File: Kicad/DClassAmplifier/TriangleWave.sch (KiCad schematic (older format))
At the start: 7 parts, among them U2 MAX4016ESA+

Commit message: Combined Board
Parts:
- C13: renamed from CF2; footprint Capacitor_SMD:C_0805_2012Metric_Pad1.18x1.45mm_HandSolder -> Capacitor_SMD:C_0603_1608Metric_Pad1.08x0.95mm_HandSolder
- C14: renamed from C5; footprint Capacitor_SMD:C_0201_0603Metric_Pad0.64x0.40mm_HandSolder -> Capacitor_SMD:C_0603_1608Metric_Pad1.08x0.95mm_HandSolder
- renumbered R4 to R22, R3 to R23, R5 to R24, R6 to R25, U2 to U4
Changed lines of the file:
@@
 $EndDescr
 $Comp
-L power:VCC #PWR015
+L power:VCC #PWR039
 U 1 1 610A2484
 P 6500 3450
-F 0 "#PWR015" H 6500 3300 50  0001 C CNN
+F 0 "#PWR039" H 6500 3300 50  0001 C CNN
 F 1 "VCC" H 6515 3623 50  0000 C CNN
 F 2 "" H 6500 3450 50  0001 C CNN
@@
 $EndComp
 $Comp
-L power:GND #PWR014
+L power:GND #PWR041
 U 1 1 610A5C03
 P 4100 4100
-F 0 "#PWR014" H 4100 3850 50  0001 C CNN
+F 0 "#PWR041" H 4100 3850 50  0001 C CNN
 F 1 "GND" H 4105 3927 50  0000 C CNN
 F 2 "" H 4100 4100 50  0001 C CNN
@@
 TRIANGLE_OUT
 $Comp
-L Device:R_Small R4
+L Device:R_Small R22
 U 1 1 610ABFC7
 P 5300 2850
-F 0 "R4" V 5104 2850 50  0000 C CNN
+F 0 "R22" V 5104 2850 50  0000 C CNN
 F 1 "2.2k" V 5195 2850 50  0000 C CNN
 F 2 "Resistor_SMD:R_0603_1608Metric_Pad0.98x0.95mm_HandSolder" H 5300 2850 50  0001 C CNN
@@
 	4100 4100 4100 3750
 $Comp
-L Device:C_Small C5
+L Device:C_Small C14
 U 1 1 610B0597
 P 6850 3650
-F 0 "C5" V 6950 3575 50  0000 L CNN
+F 0 "C14" V 6950 3575 50  0000 L CNN
 F 1 "10n" V 7025 3575 50  0000 L CNN
-F 2 "Capacitor_SMD:C_0201_0603Metric_Pad0.64x0.40mm_HandSolder" H 6850 3650 50  0001 C CNN
+F 2 "Capacitor_SMD:C_0603_1608Metric_Pad1.08x0.95mm_HandSolder" H 6850 3650 50  0001 C CNN
 F 3 "~" H 6850 3650 50  0001 C CNN
 	1    6850 3650
@@
 	7000 3550 7100 3550
 $Comp
-L Device:R_Small R5
+L Device:R_Small R24
 U 1 1 610B770E
 P 5300 4600
-F 0 "R5" V 5104 4600 50  0000 C CNN
+F 0 "R24" V 5104 4600 50  0000 C CNN
 F 1 "12k" V 5195 4600 50  0000 C CNN
 F 2 "Resistor_SMD:R_0603_1608Metric_Pad0.98x0.95mm_HandSolder" H 5300 4600 50  0001 C CNN
@@
 	3900 3450 3500 3450
 $Comp
-L Device:R_Small R3
+L Device:R_Small R23
 U 1 1 610B9D20
 P 3500 3550
-F 0 "R3" H 3559 3596 50  0000 L CNN
+F 0 "R23" H 3559 3596 50  0000 L CNN
 F 1 "27k" H 3559 3505 50  0000 L CNN
 F 2 "Resistor_SMD:R_0603_1608Metric_Pad0.98x0.95mm_HandSolder" H 3500 3550 50  0001 C CNN
@@
 	6600 3650 6750 3650
 $Comp
-L Device:R_Small R6
+L Device:R_Small R25
 U 1 1 6110AB92
 P 5300 4950
-F 0 "R6" V 5104 4950 50  0000 C CNN
+F 0 "R25" V 5104 4950 50  0000 C CNN
 F 1 "12k" V 5195 4950 50  0000 C CNN
 F 2 "Resistor_SMD:R_0603_1608Metric_Pad0.98x0.95mm_HandSolder" H 5300 4950 50  0001 C CNN
@@
 	5050 4750 5050 4950
 $Comp
-L DClassAmplifier-rescue:MAX4016ESA+-MAX4016ESA U2
+L DClassAmplifier-rescue:MAX4016ESA+-MAX4016ESA U4
 U 1 1 610FB9E0
 P 4100 3450
-F 0 "U2" H 5300 3837 60  0000 C CNN
+F 0 "U4" H 5300 3837 60  0000 C CNN
 F 1 "MAX4016ESA+" H 5300 3731 60  0000 C CNN
 F 2 "MAX4016ESA:MAX4016ESA&plus_" H 5300 3690 60  0001 C CNN
@@
 $EndComp
 $Comp
-L Device:C_Small CF?
+L Device:C_Small C?
 U 1 1 611DAEFE
 P 6600 3450
-AR Path="/610C616D/611DAEFE" Ref="CF?"  Part="1"
-AR Path="/611D4178/611DAEFE" Ref="CF?"  Part="1"
-AR Path="/6109BB03/611DAEFE" Ref="CF2"  Part="1"
-F 0 "CF2" V 6371 3450 50  0000 C CNN
+AR Path="/610C616D/611DAEFE" Ref="C?"  Part="1"
+AR Path="/611D4178/611DAEFE" Ref="C?"  Part="1"
+AR Path="/6109BB03/611DAEFE" Ref="C13"  Part="1"
+F 0 "C13" V 6371 3450 50  0000 C CNN
 F 1 "100n" V 6462 3450 50  0000 C CNN
-F 2 "Capacitor_SMD:C_0805_2012Metric_Pad1.18x1.45mm_HandSolder" H 6600 3450 50  0001 C CNN
+F 2 "Capacitor_SMD:C_0603_1608Metric_Pad1.08x0.95mm_HandSolder" H 6600 3450 50  0001 C CNN
 F 3 "~" H 6600 3450 50  0001 C CNN
 	1    6600 3450
@@
 $EndComp
 $Comp
-L power:GND #PWR?
+L power:GND #PWR040
 U 1 1 611DAF04
 P 6700 3450
-F 0 "#PWR?" H 6700 3200 50  0001 C CNN
+F 0 "#PWR040" H 6700 3200 50  0001 C CNN
 F 1 "GND" H 6705 3277 50  0000 C CNN
 F 2 "" H 6700 3450 50  0001 C CNN

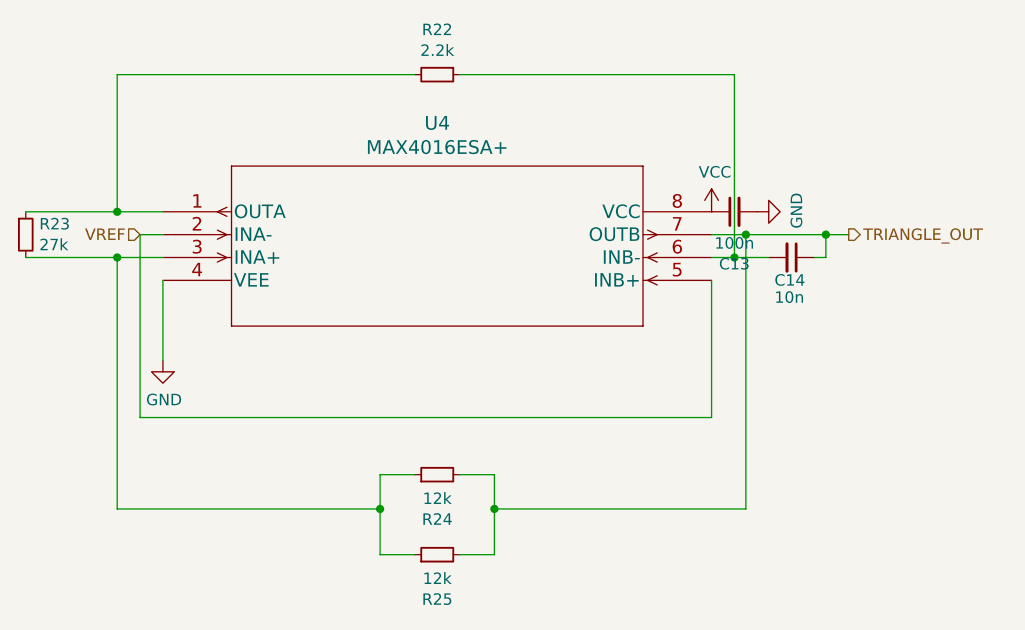
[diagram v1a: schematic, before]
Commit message: Add 10V Reg and Reroute
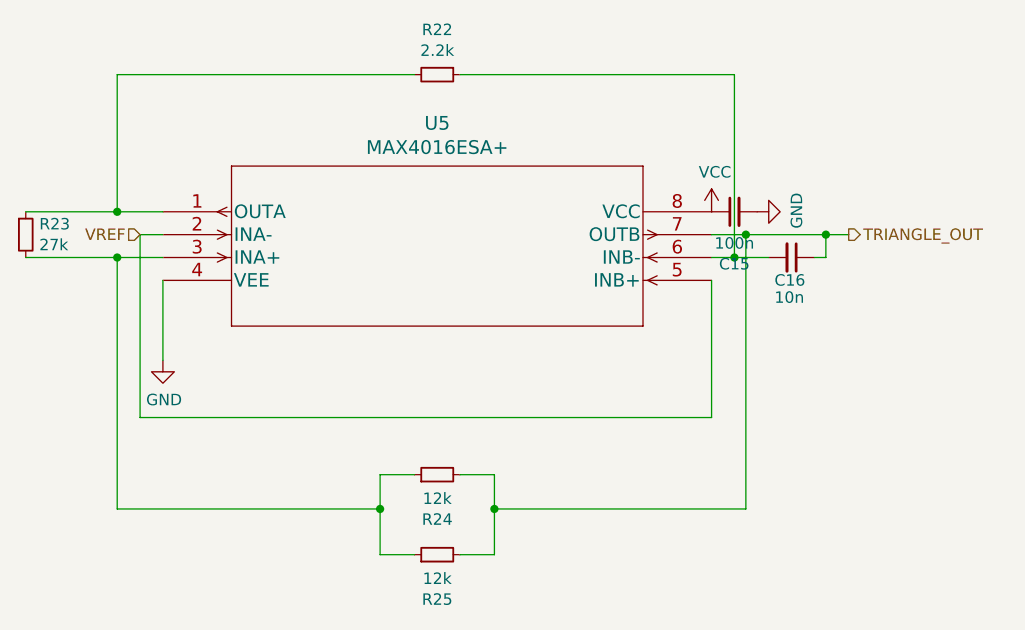
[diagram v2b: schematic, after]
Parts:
- renumbered C13 to C15, C14 to C16, U4 to U5
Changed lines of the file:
@@
 $EndDescr
 $Comp
-L power:VCC #PWR039
+L power:VCC #PWR042
 U 1 1 610A2484
 P 6500 3450
-F 0 "#PWR039" H 6500 3300 50  0001 C CNN
+F 0 "#PWR042" H 6500 3300 50  0001 C CNN
 F 1 "VCC" H 6515 3623 50  0000 C CNN
 F 2 "" H 6500 3450 50  0001 C CNN
@@
 $EndComp
 $Comp
-L power:GND #PWR041
+L power:GND #PWR044
 U 1 1 610A5C03
 P 4100 4100
-F 0 "#PWR041" H 4100 3850 50  0001 C CNN
+F 0 "#PWR044" H 4100 3850 50  0001 C CNN
 F 1 "GND" H 4105 3927 50  0000 C CNN
 F 2 "" H 4100 4100 50  0001 C CNN
@@
 	4100 4100 4100 3750
 $Comp
-L Device:C_Small C14
+L Device:C_Small C16
 U 1 1 610B0597
 P 6850 3650
-F 0 "C14" V 6950 3575 50  0000 L CNN
+F 0 "C16" V 6950 3575 50  0000 L CNN
 F 1 "10n" V 7025 3575 50  0000 L CNN
 F 2 "Capacitor_SMD:C_0603_1608Metric_Pad1.08x0.95mm_HandSolder" H 6850 3650 50  0001 C CNN
@@
 	5050 4750 5050 4950
 $Comp
-L DClassAmplifier-rescue:MAX4016ESA+-MAX4016ESA U4
+L DClassAmplifier-rescue:MAX4016ESA+-MAX4016ESA U5
 U 1 1 610FB9E0
 P 4100 3450
-F 0 "U4" H 5300 3837 60  0000 C CNN
+F 0 "U5" H 5300 3837 60  0000 C CNN
 F 1 "MAX4016ESA+" H 5300 3731 60  0000 C CNN
 F 2 "MAX4016ESA:MAX4016ESA&plus_" H 5300 3690 60  0001 C CNN
@@
 AR Path="/610C616D/611DAEFE" Ref="C?"  Part="1"
 AR Path="/611D4178/611DAEFE" Ref="C?"  Part="1"
-AR Path="/6109BB03/611DAEFE" Ref="C13"  Part="1"
-F 0 "C13" V 6371 3450 50  0000 C CNN
+AR Path="/6109BB03/611DAEFE" Ref="C15"  Part="1"
+F 0 "C15" V 6371 3450 50  0000 C CNN
 F 1 "100n" V 6462 3450 50  0000 C CNN
 F 2 "Capacitor_SMD:C_0603_1608Metric_Pad1.08x0.95mm_HandSolder" H 6600 3450 50  0001 C CNN
@@
 $EndComp
 $Comp
-L power:GND #PWR040
+L power:GND #PWR043
 U 1 1 611DAF04
 P 6700 3450
-F 0 "#PWR040" H 6700 3200 50  0001 C CNN
+F 0 "#PWR043" H 6700 3200 50  0001 C CNN
 F 1 "GND" H 6705 3277 50  0000 C CNN
 F 2 "" H 6700 3450 50  0001 C CNN
